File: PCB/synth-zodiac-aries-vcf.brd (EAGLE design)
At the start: 160 x 100 mm, 75 parts, among them J4 6.35MM JACK, Q2 PMP4201, Q3 PMP4201, Q4 PMP4201, Q5 PMP4201, Q6 PMP4201, Q7 BC847BPN, Q8 PNP, U2 LM13700, U6 NE5532A

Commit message: Snapshot of designs so far.
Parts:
- removed AUD_OUT, TP1, TP17: TPTHD-038, con-testpoints:THD-038MIL-X1
- removed C22, C23, C24, C25, C27, C29, C30, C34, C35: 0.1uF, rlc:0603-CAP
- removed C26: 100uF/25V, rlc:CAP_ALUM_SMT_6.3
- removed C28, C31, C32: 2.2uF, rlc:0603-CAP
- removed C33: 2.2uF/16V, rlc:CAP_ALUM_SMT_4
- removed GND_VCA: TPTHD-SCOPE-LOOP, con-testpoints:TP-2P-THD
- removed J4: 6.35MM JACK, con-trs:TE-CK-6.35-29B
- removed JMP1, JMP3, JMP4, JMP5, JMP6, JMP7: NP, rlc:0603-RES
- removed JMP57, JMP58, JMP62: 0, rlc:0603-RES
- removed Q8: PNP, transistor-bjt:SOT-23
- removed R26, R29, R32, R34: 1.0K, rlc:0603-RES
- removed R30, R31: 2.74K, rlc:0603-RES
- removed R33, R44, R51: 12.1K, rlc:0603-RES
- removed R35, R41: 68.1K, rlc:0603-RES
- removed R36, R47: 33.2K, rlc:0603-RES
- removed R37, R45: 100K, rlc:0603-RES
- removed R38: 47.5K, rlc:0603-RES
- removed R39, R40, R49: 4.99K, rlc:0603-RES
- removed R42: 100, rlc:0603-RES
- removed R43: 6.81K, rlc:0603-RES
- removed R46, R48: 681R, rlc:0603-RES
- removed R50, R54, R55: 10.0K, rlc:0603-RES
- removed R52: 475R, rlc:0603-RES
- removed R53: 4.75M, rlc:0603-RES
- removed R56: 499K, rlc:0603-RES
- removed U2: LM13700, op-amp:SO16
- removed VR3, VR4: 10K, rlc:ALPS_RK09D113
- removed VR7: 10K, rlc:TRIM_BOURNS_TC33X
- added C1, C8, C9: 2.2uF, rlc:0603-CAP
- added C10, C11, C2, C3, C4, C5, C7: 0.1uF, rlc:0603-CAP
- added C6: 100uF/25V, rlc:CAP_ALUM_SMT_6.3
- added CAL: 10K, rlc:TRIM_BOURNS_TC33X
- added CONST: Aries, circuit-monkey-zodiac:ARIES-CONST
- added CUTOFF, RES: 10K, rlc:POT-RV9110
- added CV_VCF, CV_VCF_MOD, MOD_MIX, TP_VCF_OUT: TPSMD-040-RND, con-testpoints:SMD-040MIL-RND
- added GLYPH: Aries, circuit-monkey-zodiac:ARIES-GLYPH
- added J1: (no value), con-jst:B4B-PH-SM4
- added MOD_IN, VCF_MOD: 2-pin, VT, SMT, con-jst:B2B-PH-SM4
- added PCB: PCB FAB, circuit-monkey-zodiac:PENTAGON-40MM-RAD
- added R1, R7: 68.1K, rlc:0603-RES
- added R10, R11, R12, R13, R15, R16, R18, R8: 1.0K, rlc:0603-RES
- added R14, R9: 2.74K, rlc:0603-RES
- added R17: 12.1K, rlc:0603-RES
- added R19: 100, rlc:0603-RES
- added R2: 47.5K, rlc:0603-RES
- added R4: 33.2K, rlc:0603-RES
- added R5, R6: 4.99K, rlc:0603-RES
- added SHORT1: NP, rlc:0603-SHORT
- JMP2: value NP -> 0
- R20: value 1.0K -> 6.81K
- R21: value 1.0K -> 12.1K
- R22, R3: value 1.0K -> 100K
- VCF_OUT: value TPTHD-038 -> 2-pin, VT, SMT; device con-testpoints:THD-038MIL-X1 -> con-jst:B2B-PH-SM4
- moved R22 103.4 mm to (38.0, 50.4), flipped to the bottom
- moved JMP2 102.1 mm to (38.0, 51.7), flipped to the bottom, turned to 180 degrees
- moved R3 99.8 mm to (25.4, 30.4), flipped to the bottom, turned to 180 degrees
- moved VCF_OUT 99.4 mm to (48.5, 53.9), flipped to the bottom, turned to 36 degrees
- moved R20 96.6 mm to (31.8, 43.4), flipped to the bottom
- moved R21 91.9 mm to (41.6, 38.4), flipped to the bottom
- moved Q2 84.2 mm to (38.0, 36.0), flipped to the bottom, turned to 270 degrees
- moved U6 82.2 mm to (38.0, 43.6), flipped to the bottom, turned to 270 degrees
- moved Q3 81.5 mm to (38.0, 34.0), flipped to the bottom, turned to 270 degrees
- moved Q4 78.9 mm to (38.0, 32.0), flipped to the bottom, turned to 270 degrees
- moved Q5 76.3 mm to (38.0, 30.0), flipped to the bottom, turned to 270 degrees
- moved Q7 75.2 mm to (38.0, 25.6), flipped to the bottom, turned to 270 degrees
- moved Q6 73.8 mm to (38.0, 28.0), flipped to the bottom, turned to 270 degrees
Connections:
- removed net AUDIO_OUT: AUD_OUT.1, J4.T, R52.2
- removed net EXP_VCA_CV: R55.1, R56.2
- removed net N$44: C28.2, Q6.1, R3.2
- removed net N$45: R46.2, U2.13
- removed net N$50: Q7.5, R34.2, R35.2, R36.2, R37.2, R38.2, TP17.1
- removed net N$51: R35.1, VR7.C
- removed net N$54: R37.1, VR3.2
- removed net N$60: R47.2, R48.2, U2.14
- removed net N$61: TP1.1, U2.15
- removed net N$62: R49.2, U2.10, U2.12
- removed net N$63: R50.2, U2.16
- removed net N$64: C33.POS, R51.2, U2.9
- removed net N$65: C33.NEG, R52.1
- removed net N$66: Q8.3, R50.1, R53.2
- removed net N$67: JMP62.2, Q8.2
- removed net N$68: JMP62.1, R54.2, R55.2
- removed net N$69: JMP1.2, U2.4
- removed net N$70: JMP3.2, U2.3
- removed net N$71: JMP5.1, U2.5
- removed net N$72: JMP2.2, U2.2
- removed net N$73: JMP4.2, U2.1
- removed net N$74: JMP6.2, U2.7
- removed net N$75: JMP7.1, U2.8
- removed net VCA_CV: R54.1
- new net CAL: CAL.C, R7.1
- new net CUTOFF: CUTOFF.C, R3.1
- new net MOD_MIX: MOD_MIX.TP, Q7.5, R2.2, R3.2, R4.2, R7.2, R8.2
- new net VCO_MIX: C1.2, Q6.1, R15.2
- net +9V: now also C10.2, CUTOFF.T, J1.1, R17.2, R9.2; no longer C29.2, C34.2, R30.2, R33.2, U2.11, VR3.3
- net -9V: now also C11.1, CUTOFF.B, J1.2, R6.1; no longer C30.1, C35.1, R39.1, R53.1, R56.1, U2.6, VR3.1
- net EXP_VCF_CV: now also CV_VCF_MOD.TP, R2.1; no longer R38.1
- net FILT(+): now also C2.2; no longer C22.2
- net FILT(-): now also C2.1; no longer C22.1
- net GND: now also C10.1, C11.2, C6.-, C7.2, J1.4, MOD_IN.2, PCB.MTG1, PCB.MTG2, PCB.MTG3, PCB.MTG4, PCB.MTG5, R14.1, R22.1, R5.2, R8.1, RES.B, VCF_MOD.2, VCF_OUT.2; no longer C26.-, C27.2, C29.1, C30.2, C34.1, C35.2, GND_VCA.1, GND_VCA.2, J4.S, Q8.1, R31.1, R34.1, R40.2, R45.1, R46.1, R48.1, R49.1, R51.1, VR3.MT1A, VR3.MT1B, VR3.MT1C, VR3.MT2A, VR3.MT2B, VR3.MT2C, VR4.1, VR4.MT1A, VR4.MT1B, VR4.MT1C, VR4.MT2A, VR4.MT2B, VR4.MT2C
- net N$32: now also R19.2, R20.1; no longer R42.2, R43.1
- net N$33: now also C8.2, JMP2.1, R22.2; no longer C31.2, JMP58.1, R45.2
- net N$34: now also R10.2, R9.1; no longer R21.2, R30.1
- net N$35: now also C3.1; no longer C23.1
- net N$36: now also C3.2; no longer C23.2
- net N$37: now also R10.1, R11.2; no longer R21.1, R22.2
- net N$38: now also C4.1; no longer C24.1
- net N$39: now also C4.2; no longer C24.2
- net N$40: now also R11.1, R12.2; no longer R22.1, R26.2
- net N$41: now also C5.1; no longer C25.1
- net N$42: now also C5.2; no longer C25.2
- net N$43: now also R12.1, R13.2; no longer R26.1, R29.2
- net N$46: now also R18.2; no longer R32.2
- net N$47: now also R18.1; no longer R32.1
- net N$48: now also C6.+, R13.1, R14.2, R15.1, R16.1; no longer C26.+, R20.1, R29.1, R3.1, R31.2
- net N$49: now also C7.1, R17.1; no longer C27.1, R33.1
- net N$52: now also CAL.T, R6.2; no longer R39.2, VR7.T
- net N$53: now also CAL.B, R5.1; no longer R40.1, VR7.B
- net N$55: now also C1.1, R1.2; no longer C28.1, R41.2
- net N$56: now also R19.1; no longer R42.1
- net N$57: now also C8.1, R20.2, R21.2; no longer C31.1, R43.2, R44.2
- net N$58: now also R21.1, RES.T; no longer R44.1, VR4.3
- net N$59: now also C9.2, RES.C; no longer C32.2, VR4.2
- net RES_INPUT: now also C9.1, R16.2; no longer C32.1, R20.2
- net VCF_IN: now also CV_VCF.TP, R1.1, SHORT1.4; no longer JMP57.2, R41.1
- net VCF_MOD: now also R4.1, VCF_MOD.1; no longer R36.1
- net VCF_OUT: now also JMP2.2, TP_VCF_OUT.TP; no longer JMP58.2, R47.1
- net VCO_OUT: now also MOD_IN.1, SHORT1.3; no longer JMP57.1
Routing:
- net -9V: track 0.00 -> 172.9 mm
- net +9V: track 0.00 -> 62.5 mm, vias 0 -> 2
- net RES_INPUT: track 0.00 -> 35.3 mm, vias 0 -> 2
- net N$57: track 0.00 -> 28.2 mm
- net N$48: track 0.00 -> 20.4 mm
- net MOD_MIX: track 0.00 -> 18.6 mm
- net VCF_OUT: track 0.00 -> 16.6 mm
- net FILT(+): track 0.00 -> 16.5 mm, vias 0 -> 2
- net VCO_MIX: track 0.00 -> 16.3 mm
- net N$59: track 0.00 -> 15.7 mm
- net VCF_IN: track 0.00 -> 14.6 mm
- net FILT(-): track 0.00 -> 14.2 mm, vias 0 -> 3
- net CAL: track 0.00 -> 12.9 mm
- net CUTOFF: track 0.00 -> 12.7 mm
- net N$35: track 0.00 -> 10.9 mm
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- added copper zone on layer 1, net GND
- added copper zone on layer 16, net GND
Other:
- board size 160 x 100 mm -> 76.1 x 72.4 mm
- board text added: "A R I E S"
- board text added: "S A T A N ' S C Y C L E W O R K S"
- board text added: "VCF"

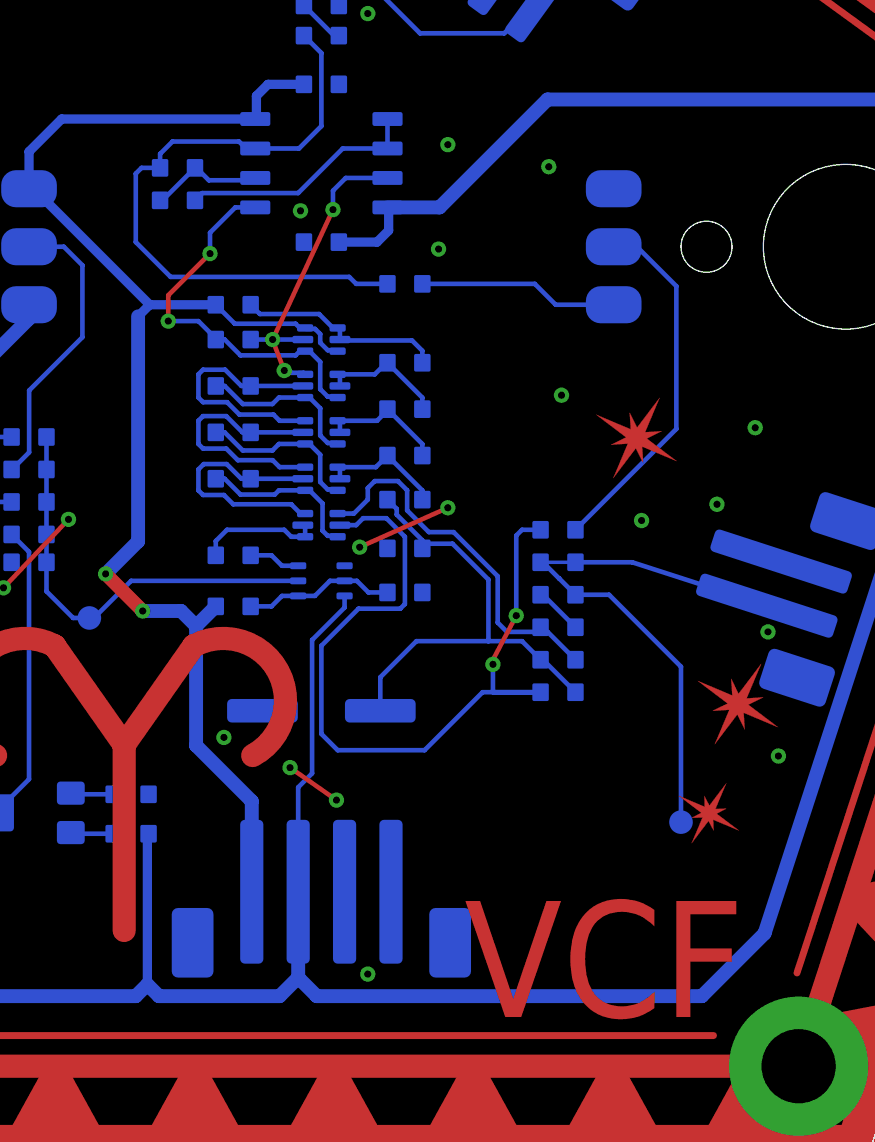
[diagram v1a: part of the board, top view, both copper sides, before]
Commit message: Almost ready for FAB.
Sagittarius was mis-spelled, renamed it.  Taurus is still WIP.
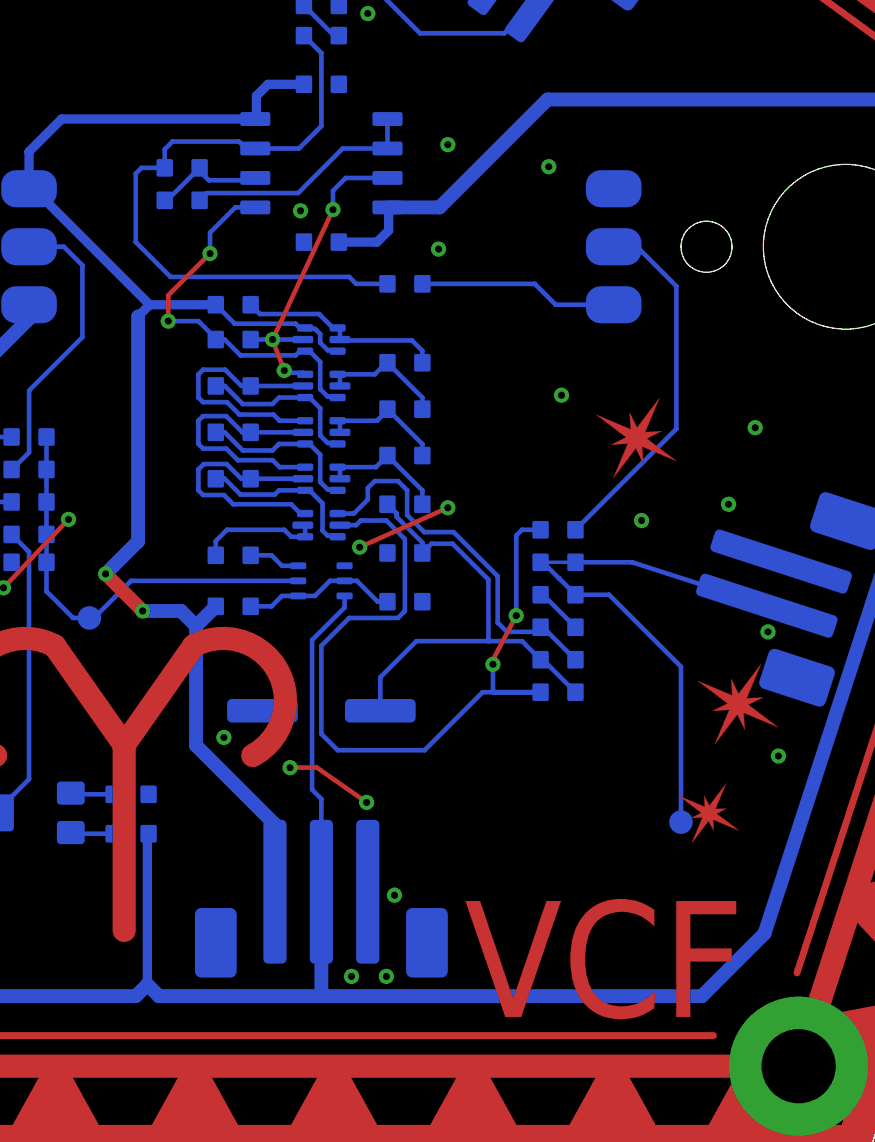
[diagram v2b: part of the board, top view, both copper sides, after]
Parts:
- removed J1: (no value), con-jst:B4B-PH-SM4
- removed Q7: BC847BPN, transistor-bjt:SOT363
- added PWR: JST, 3P, VT, SMT, con-jst:B3B-PH-SM4
- added Q1: PMP4201, transistor-bjt:SOT666
- Q6: value PMP4201 -> BC847BPN; device transistor-bjt:SOT666 -> transistor-bjt:SOT363
- moved Q6 2.40 mm to (38.0, 25.6)
- moved Q2 2.00 mm to (38.0, 34.0)
- moved Q3 2.00 mm to (38.0, 32.0)
- moved Q4 2.00 mm to (38.0, 30.0)
- moved Q5 2.00 mm to (38.0, 28.0)
- moved C7 0.40 mm to (41.6, 24.7)
- moved R13 0.20 mm to (41.6, 28.9)
- moved R14 0.20 mm to (41.6, 26.8)
- moved R19 0.20 mm to (32.0, 42.0)
- moved R20 0.20 mm to (32.0, 43.4)
- renumbered MOD_IN to VCO_IN, SHORT1 to JMP1, U6 to U1, VCF_MOD to VCF_MOD_IN, VCF_OUT to VCF2VCA
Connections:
- net +9V: now also PWR.1, Q1.3, Q1.6; no longer J1.1, Q2.3, Q2.6
- net -9V: now also PWR.2, Q6.3; no longer J1.2, Q7.3
- net FILT(+): now also Q1.4, Q2.3; no longer Q2.4, Q3.3
- net FILT(-): now also Q1.5, Q2.6; no longer Q2.5, Q3.6
- net GND: now also PWR.3, Q6.1; no longer J1.4, Q7.1
- net MOD_MIX: now also Q6.5; no longer Q7.5
- net N$34: now also Q1.1, Q1.2; no longer Q2.1, Q2.2
- net N$35: now also Q2.5, Q3.6; no longer Q3.5, Q4.6
- net N$36: now also Q2.4, Q3.3; no longer Q3.4, Q4.3
- net N$37: now also Q2.1, Q2.2; no longer Q3.1, Q3.2
- net N$38: now also Q3.5, Q4.6; no longer Q4.5, Q5.6
- net N$39: now also Q3.4, Q4.3; no longer Q4.4, Q5.3
- net N$40: now also Q3.1, Q3.2; no longer Q4.1, Q4.2
- net N$41: now also Q4.5, Q5.6; no longer Q5.5, Q6.6
- net N$42: now also Q4.4, Q5.3; no longer Q5.4, Q6.3
- net N$43: now also Q4.1, Q4.2; no longer Q5.1, Q5.2
- net N$46: now also Q5.4, Q5.5; no longer Q6.4, Q6.5
- net N$47: now also Q6.6; no longer Q7.6
- net N$49: now also Q6.2, Q6.4; no longer Q7.2, Q7.4
- net RES_INPUT: now also Q5.2; no longer Q6.2
- net VCO_MIX: now also Q5.1; no longer Q6.1
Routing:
- net GND: track 10.7 -> 12.0 mm, vias 24 -> 26
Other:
- board text added: "Rev. A"

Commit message: Work in progress for rev A,  VCO rev.B
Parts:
- removed CV_VCF_MOD: TPSMD-040-RND, con-testpoints:SMD-040MIL-RND
- removed JMP2: 0, rlc:0603-RES
- added C_0-5, C_GND: PADSMD-070X070, con-testpoints:SMD-070MIL
- added R23: 150K, rlc:0603-RES
- added R24: 47K, rlc:0603-RES
- PWR: value JST, 3P, VT, SMT -> JST SM 3P; device con-jst:B3B-PH-SM4 -> con-jst:BM03B-SRSS-TB
- R2: value 47.5K -> 150K
- VCF2VCA, VCF_MOD_IN, VCO_IN: value 2-pin, VT, SMT -> JST, SH, 2P; device con-jst:B2B-PH-SM4 -> con-jst:BM02B-SRSS-TB
- moved R6 8.05 mm to (22.7, 10.9), turned to 90 degrees
- moved R5 7.71 mm to (24.4, 10.9), turned to 270 degrees
- moved CV_VCF 3.81 mm to (52.0, 18.7)
- moved VCO_IN 2.64 mm to (58.5, 27.2)
- moved GLYPH 2.50 mm to (27.0, 17.8)
- moved VCF2VCA 2.30 mm to (48.6, 51.6)
- moved VCF_MOD_IN 2.28 mm to (17.3, 28.0)
- moved CAL 1.96 mm to (23.5, 15.1), turned to 0 degrees
- moved R2 1.80 mm to (25.4, 33.6)
- moved PWR 1.75 mm to (38.4, 11.7)
- moved C11 1.56 mm to (36.8, 39.2)
- moved C10 1.42 mm to (36.9, 46.1)
- moved R19 1.42 mm to (30.9, 41.1)
- moved R20 1.42 mm to (30.9, 42.5)
- moved U1 1.42 mm to (36.9, 42.7)
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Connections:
- net VCO_OUT renamed FROM_VCO
- removed net EXP_VCF_CV: CV_VCF_MOD.TP, R2.1
- removed net N$33: C8.2, JMP2.1, R22.2
- new net CUT_5: C_0-5.1, R2.1, R23.2, R24.2
- net +9V: now also R2.2
- net CUTOFF: now also R23.1
- net GND: now also C_GND.1, R24.1
- net MOD_MIX: no longer R2.2
- net VCF_OUT: now also C8.2, R22.2; no longer JMP2.2
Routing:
- net CUT_5: track 0.00 -> 28.3 mm
- net -9V: track 173.0 -> 157.3 mm, vias 0 -> 2
- net GND: track 12.0 -> 0.00 mm, vias 26 -> 39
- net EXP_VCF_CV: track 7.58 -> 0.00 mm
- net CAL: track 12.9 -> 18.1 mm
- net CUTOFF: track 12.7 -> 17.5 mm
- net VCF_IN: track 14.6 -> 10.5 mm
- net +9V: track 62.9 -> 66.7 mm, vias 2 -> 0
- net N$33: track 3.34 -> 0.00 mm
- net N$59: track 15.7 -> 18.5 mm
- net RES_INPUT: track 35.3 -> 32.7 mm
- net FROM_VCO: track 8.54 -> 11.0 mm
- net MOD_MIX: track 18.6 -> 16.6 mm, vias 0 -> 2
- net FILT(+): track 16.5 -> 15.1 mm
- net N$57: track 28.3 -> 29.6 mm
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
